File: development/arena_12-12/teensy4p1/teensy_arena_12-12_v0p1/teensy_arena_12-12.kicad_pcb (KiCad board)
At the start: 4 copper layers, 228.6 x 228.6 mm, 51 parts, among them J1 Barrel_Jack, J2 Conn_01x04, J3 Conn_01x04, P1 CONN15, P10 CONN15, P11 CONN15, P12 CONN15, P2 CONN15, P3 CONN15, P4 CONN15, P5 CONN15, P6 CONN15, P7 CONN15, P8 CONN15, P9 CONN15, Q2 MOSFET_NCHAN, SW1 SW_SPDT, U1 TXB0108PW, U18 Teensy4.1, U2 TXB0108PW, U3 TXB0108PW, U4 TXB0108PW, U5 TXB0108PW

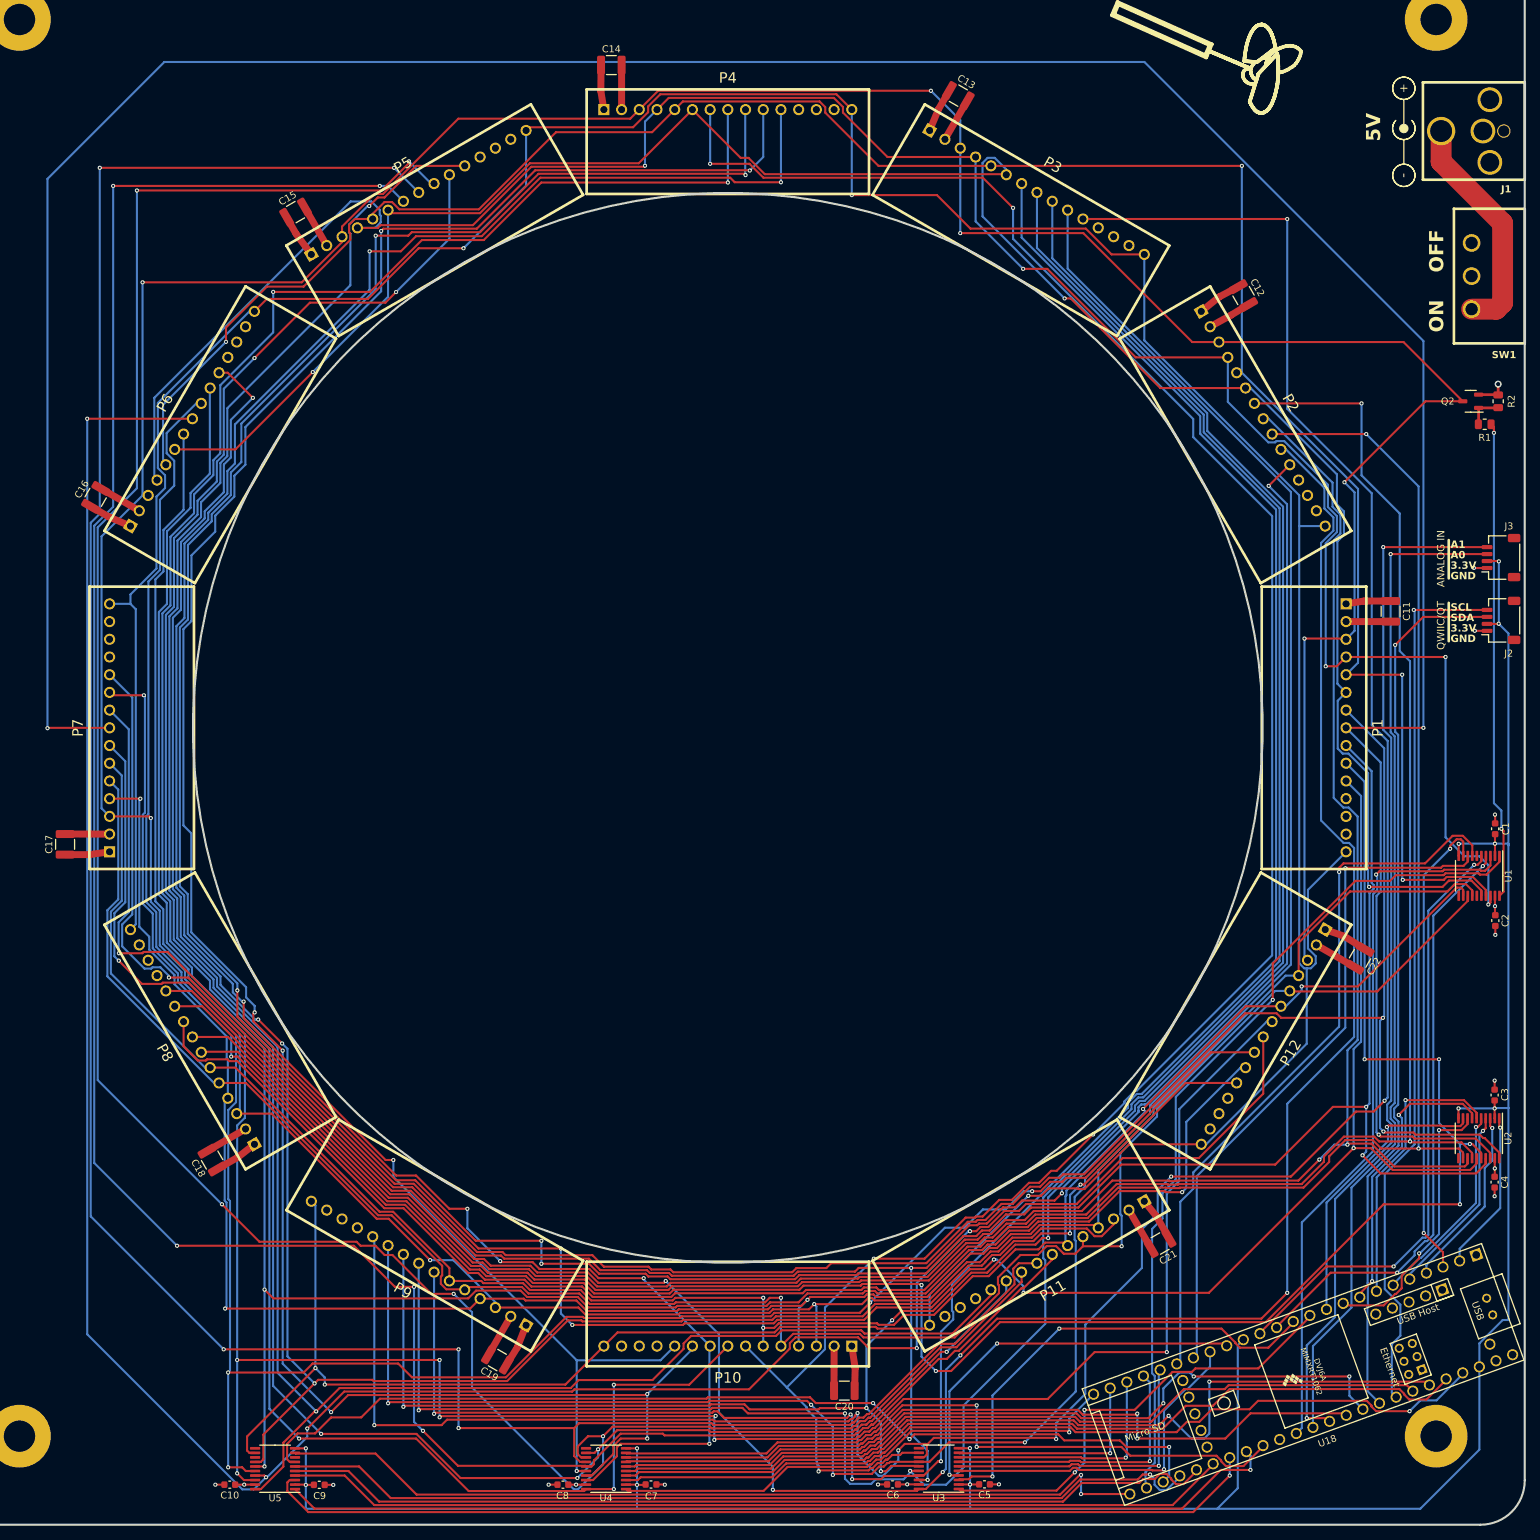
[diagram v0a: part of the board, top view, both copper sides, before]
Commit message: More work on schematic for 12-12 teensy arena.
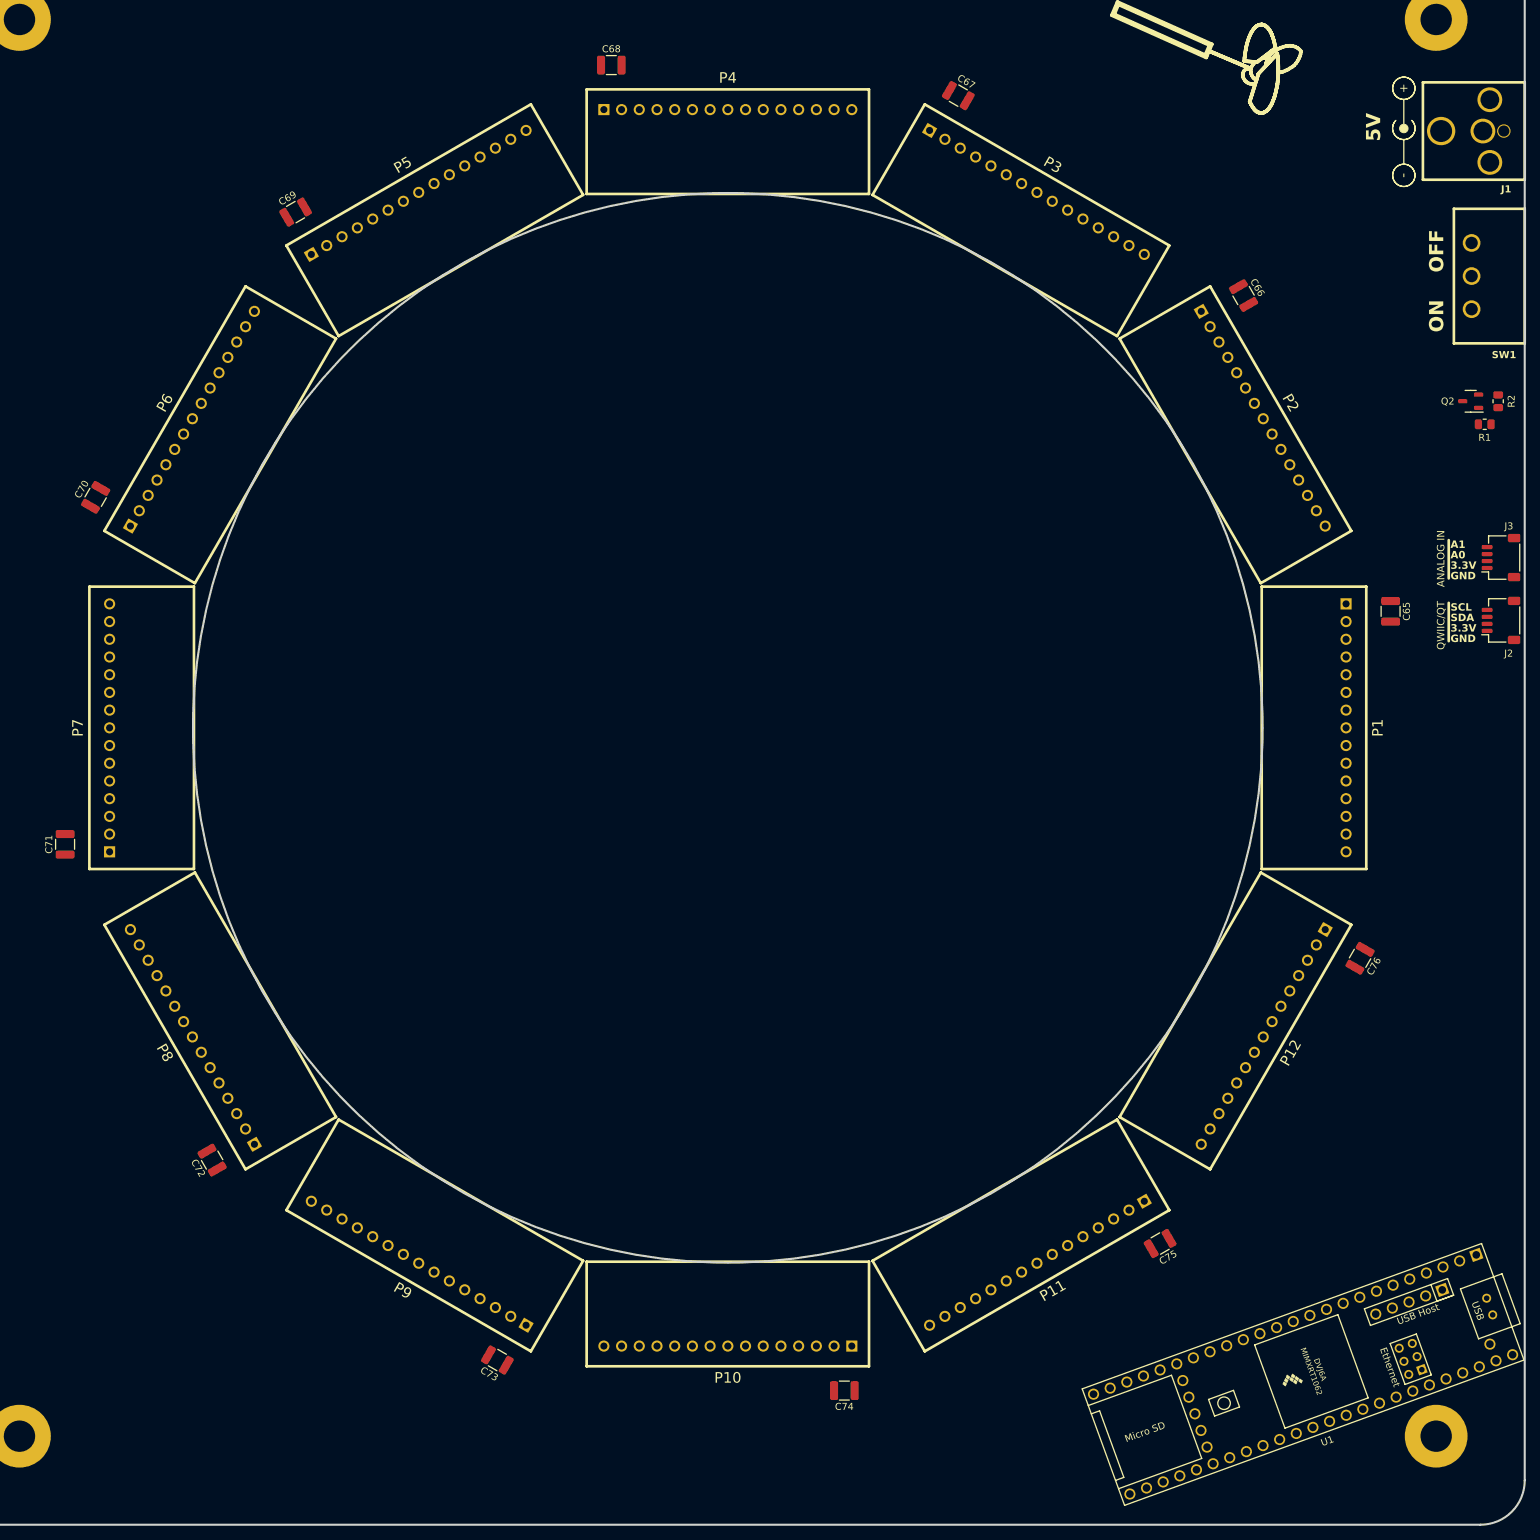
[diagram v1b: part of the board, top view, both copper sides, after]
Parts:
- removed C1, C10, C2, C3, C4, C5, C6, C7, C8, C9: 0.1uF, Capacitor_SMD:C_0603_1608Metric
- removed the U1 at (285.6, 199.0)
- removed U2, U3, U4, U5: TXB0108PW, Package_SO:TSSOP-20_4.4x6.5mm_P0.65mm
- renumbered C11 to C65, C12 to C66, C13 to C67, C14 to C68, C15 to C69, C16 to C70, C17 to C71, C18 to C72, C19 to C73, C20 to C74, C21 to C75, C22 to C76, U18 to U1
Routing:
- net /Level Shifters/PAN5V.EXT_INT: track 618.7 -> 0.00 mm, vias 5 -> 0
- net /Panel Headers/RESET: track 613.6 -> 0.00 mm, vias 8 -> 0
- net /Level Shifters/PAN5V.CS_01: track 453.8 -> 0.00 mm, vias 3 -> 0
- net +3.3V: track 394.0 -> 0.00 mm, vias 12 -> 0
- net /Level Shifters/PAN5V.CS_14: track 380.7 -> 0.00 mm, vias 7 -> 0
- net /Level Shifters/PAN5V.CS_21: track 370.7 -> 0.00 mm, vias 5 -> 0
- net /Level Shifters/PAN5V.CS_26: track 365.6 -> 0.00 mm, vias 5 -> 0
- net /Level Shifters/PAN5V.CS_25: track 364.2 -> 0.00 mm, vias 7 -> 0
- net /Level Shifters/PAN5V.CS_20: track 364.1 -> 0.00 mm, vias 5 -> 0
- net /Level Shifters/PAN5V.CS_22: track 361.9 -> 0.00 mm, vias 5 -> 0
- net /Level Shifters/PAN5V.CS_03: track 354.9 -> 0.00 mm, vias 8 -> 0
- net /Level Shifters/PAN5V.CS_08: track 348.9 -> 0.00 mm, vias 5 -> 0
- net /Level Shifters/PAN5V.CS_16: track 343.3 -> 0.00 mm, vias 5 -> 0
- net /Level Shifters/PAN5V.CS_27: track 335.3 -> 0.00 mm, vias 4 -> 0
- net /Level Shifters/PAN5V.CS_04: track 334.9 -> 0.00 mm, vias 6 -> 0
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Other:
- copper layers 4 -> 6

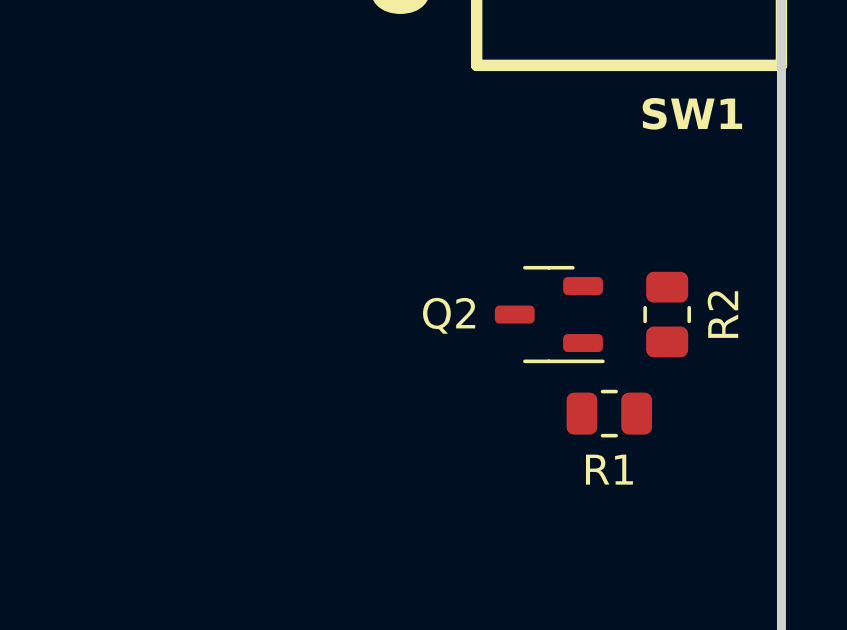
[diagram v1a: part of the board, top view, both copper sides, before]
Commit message: Reworked schematic for 12-12 teensy arena w/o regulators some more.
Worked on foot print assignmets. Started replacing some of the single
schmitt triggers with equivalent dual versions to reduce component
count.
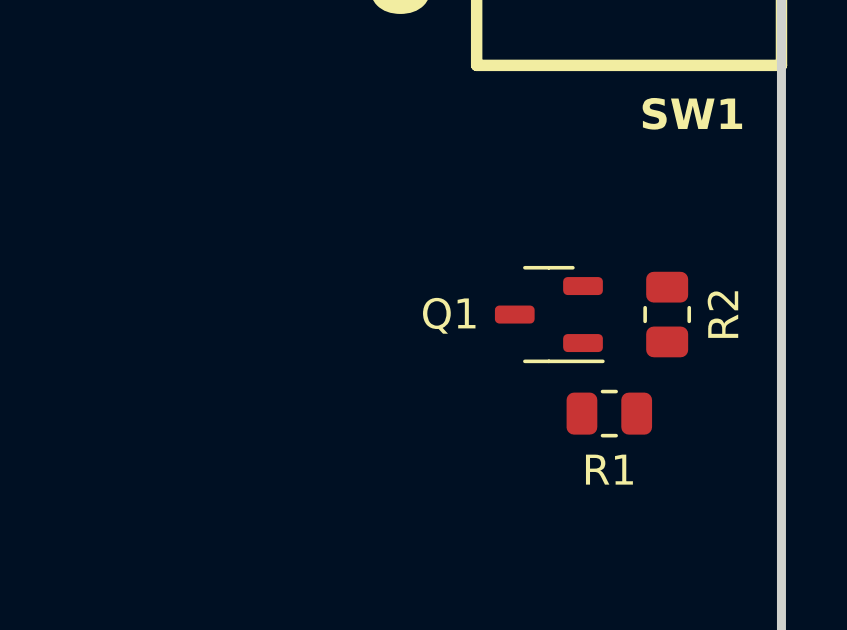
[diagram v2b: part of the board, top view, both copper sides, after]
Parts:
- renumbered Q2 to Q1
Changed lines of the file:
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@@
 		(descr "SOT, 3 Pin (https://www.jedec.org/sites/default/files/docs/Mo-178D.PDF inferred 3-pin variant), generated with kicad-footprint-generator ipc_gullwing_generator.py")
 		(tags "SOT TO_SOT_SMD")
-		(property "Reference" "Q2"
+		(property "Reference" "Q1"
 			(at 3.2965 0 0)
 			(layer "F.SilkS")
@@
 			(at 0 2.4 0)
 			(layer "F.Fab")
+			(hide yes)
 			(effects
 				(font
@@
 			(at 0 1.65 90)
 			(layer "F.Fab")
+			(hide yes)
 			(effects
 				(font
@@
 		)
 		(property "Footprint" ""
-			(at 0 0 -90)
+			(at 0 0 90)
 			(layer "F.Fab")
 			(hide yes)
@@
 		)
 		(property "Datasheet" ""
-			(at 0 0 -90)
+			(at 0 0 90)
 			(layer "F.Fab")
 			(hide yes)
@@
 		)
 		(property "Description" "Resistor"
-			(at 0 0 -90)
+			(at 0 0 90)
 			(layer "F.Fab")
 			(hide yes)

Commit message: Finished initial schematic for 12-12 teensy 4.1 arena w/o vreg.
Finished footprint assignments and started working on layout changes.
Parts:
- added C1: 0.1uF, Capacitor_SMD:C_0603_1608Metric, F.Cu at (-13.2, 115.5)
- added C10: 0.1uF, Capacitor_SMD:C_0603_1608Metric, F.Cu at (-71.9, 135.6)
- added C11: 0.1uF, Capacitor_SMD:C_0603_1608Metric, F.Cu at (-71.9, 138.1)
- added C12: 0.1uF, Capacitor_SMD:C_0603_1608Metric, F.Cu at (-71.9, 140.6)
- added C13: 0.1uF, Capacitor_SMD:C_0603_1608Metric, F.Cu at (-71.9, 143.1)
- added C14: 0.1uF, Capacitor_SMD:C_0603_1608Metric, F.Cu at (-71.9, 145.6)
- added C15: 0.1uF, Capacitor_SMD:C_0603_1608Metric, F.Cu at (-71.9, 148.1)
- added C16: 0.1uF, Capacitor_SMD:C_0603_1608Metric, F.Cu at (-71.9, 150.6)
- added C17: 0.1uF, Capacitor_SMD:C_0603_1608Metric, F.Cu at (-67.9, 115.5)
- added C18: 0.1uF, Capacitor_SMD:C_0603_1608Metric, F.Cu at (-67.9, 118.0)
- added C19: 0.1uF, Capacitor_SMD:C_0603_1608Metric, F.Cu at (-67.9, 120.5)
- added C2: 0.1uF, Capacitor_SMD:C_0603_1608Metric, F.Cu at (-71.9, 115.5)
- added C20: 0.1uF, Capacitor_SMD:C_0603_1608Metric, F.Cu at (-67.9, 123.0)
- added C21: 0.1uF, Capacitor_SMD:C_0603_1608Metric, F.Cu at (-67.9, 125.5)
- added C22: 0.1uF, Capacitor_SMD:C_0603_1608Metric, F.Cu at (-67.9, 128.0)
- added C23: 0.1uF, Capacitor_SMD:C_0603_1608Metric, F.Cu at (-67.9, 130.5)
- added C24: 0.1uF, Capacitor_SMD:C_0603_1608Metric, F.Cu at (-67.9, 133.1)
- added C25: 0.1uF, Capacitor_SMD:C_0603_1608Metric, F.Cu at (-67.9, 135.6)
- added C26: 0.1uF, Capacitor_SMD:C_0603_1608Metric, F.Cu at (-67.9, 138.1)
- added C27: 0.1uF, Capacitor_SMD:C_0603_1608Metric, F.Cu at (-67.9, 140.6)
- added C28: 0.1uF, Capacitor_SMD:C_0603_1608Metric, F.Cu at (-67.9, 143.1)
- added C29: 0.1uF, Capacitor_SMD:C_0603_1608Metric, F.Cu at (-67.9, 145.6)
- added C3: 0.1uF, Capacitor_SMD:C_0603_1608Metric, F.Cu at (-71.9, 118.0)
- added C30: 0.1uF, Capacitor_SMD:C_0603_1608Metric, F.Cu at (-67.9, 148.1)
- added C31: 0.1uF, Capacitor_SMD:C_0603_1608Metric, F.Cu at (-67.9, 150.6)
- added C32: 0.1uF, Capacitor_SMD:C_0603_1608Metric, F.Cu at (-63.8, 115.5)
- added C33: 0.1uF, Capacitor_SMD:C_0603_1608Metric, F.Cu at (-63.8, 118.0)
- added C34: 0.1uF, Capacitor_SMD:C_0603_1608Metric, F.Cu at (-63.8, 120.5)
- added C35: 0.1uF, Capacitor_SMD:C_0603_1608Metric, F.Cu at (-63.8, 123.0)
- added C36: 0.1uF, Capacitor_SMD:C_0603_1608Metric, F.Cu at (-63.8, 125.5)
- added C37: 0.1uF, Capacitor_SMD:C_0603_1608Metric, F.Cu at (-63.8, 128.0)
- added C38: 0.1uF, Capacitor_SMD:C_0603_1608Metric, F.Cu at (-63.8, 130.5)
- added C39: 0.1uF, Capacitor_SMD:C_0603_1608Metric, F.Cu at (-63.8, 133.1)
- added C4: 0.1uF, Capacitor_SMD:C_0603_1608Metric, F.Cu at (-71.9, 120.5)
- added C40: 0.1uF, Capacitor_SMD:C_0603_1608Metric, F.Cu at (-63.8, 135.6)
- added C41: 0.1uF, Capacitor_SMD:C_0603_1608Metric, F.Cu at (-63.8, 138.1)
- added C42: 0.1uF, Capacitor_SMD:C_0603_1608Metric, F.Cu at (-63.8, 140.6)
- added C43: 0.1uF, Capacitor_SMD:C_0603_1608Metric, F.Cu at (-63.8, 143.1)
- added C44: 0.1uF, Capacitor_SMD:C_0603_1608Metric, F.Cu at (-63.8, 145.6)
- added C45: 0.1uF, Capacitor_SMD:C_0603_1608Metric, F.Cu at (-63.8, 148.1)
- added C46: 0.1uF, Capacitor_SMD:C_0603_1608Metric, F.Cu at (-63.8, 150.6)
- added C47: 0.1uF, Capacitor_SMD:C_0603_1608Metric, F.Cu at (-71.9, 70.8)
- added C48: 0.1uF, Capacitor_SMD:C_0603_1608Metric, F.Cu at (-71.9, 73.3)
- added C49: 0.1uF, Capacitor_SMD:C_0603_1608Metric, F.Cu at (-71.9, 75.8)
- added C5: 0.1uF, Capacitor_SMD:C_0603_1608Metric, F.Cu at (-71.9, 123.0)
- added C50: 0.1uF, Capacitor_SMD:C_0603_1608Metric, F.Cu at (-71.9, 78.3)
- added C51: 0.1uF, Capacitor_SMD:C_0603_1608Metric, F.Cu at (-71.9, 80.9)
- added C52: 0.1uF, Capacitor_SMD:C_0603_1608Metric, F.Cu at (-71.9, 83.4)
- added C53: 0.1uF, Capacitor_SMD:C_0603_1608Metric, F.Cu at (-71.9, 85.9)
- added C54: 0.1uF, Capacitor_SMD:C_0603_1608Metric, F.Cu at (-71.9, 88.4)
- added C55: 0.1uF, Capacitor_SMD:C_0603_1608Metric, F.Cu at (-71.9, 90.9)
- added C56: 0.1uF, Capacitor_SMD:C_0603_1608Metric, F.Cu at (-71.9, 93.4)
- added C57: 0.1uF, Capacitor_SMD:C_0603_1608Metric, F.Cu at (-71.9, 95.9)
- added C58: 0.1uF, Capacitor_SMD:C_0603_1608Metric, F.Cu at (-71.9, 98.4)
- added C59: 0.1uF, Capacitor_SMD:C_0603_1608Metric, F.Cu at (-71.9, 100.9)
- added C6: 0.1uF, Capacitor_SMD:C_0603_1608Metric, F.Cu at (-71.9, 125.5)
- added C60: 0.1uF, Capacitor_SMD:C_0603_1608Metric, F.Cu at (-71.9, 103.4)
- added C61: 0.1uF, Capacitor_SMD:C_0603_1608Metric, F.Cu at (-71.9, 106.0)
- added C62: 0.1uF, Capacitor_SMD:C_0603_1608Metric, F.Cu at (-71.9, 108.5)
- added C63: 0.1uF, Capacitor_SMD:C_0603_1608Metric, F.Cu at (-71.9, 111.0)
- added C64: 0.1uF, Capacitor_SMD:C_0603_1608Metric, F.Cu at (-67.9, 70.8)
- added C65: 0.1uF, Capacitor_SMD:C_0603_1608Metric, F.Cu at (-67.9, 73.3)
- added C66: 0.1uF, Capacitor_SMD:C_0603_1608Metric, F.Cu at (-67.9, 75.8)
- added C67: 0.1uF, Capacitor_SMD:C_0603_1608Metric, F.Cu at (-67.9, 78.3)
- added C68: 0.1uF, Capacitor_SMD:C_0603_1608Metric, F.Cu at (-67.9, 80.9)
- added C69: 0.1uF, Capacitor_SMD:C_0603_1608Metric, F.Cu at (-67.9, 83.4)
- added C7: 0.1uF, Capacitor_SMD:C_0603_1608Metric, F.Cu at (-71.9, 128.0)
- added C70: 0.1uF, Capacitor_SMD:C_0603_1608Metric, F.Cu at (-67.9, 85.9)
- added C71: 0.1uF, Capacitor_SMD:C_0603_1608Metric, F.Cu at (-67.9, 88.4)
- added C72: 0.1uF, Capacitor_SMD:C_0603_1608Metric, F.Cu at (-67.9, 90.9)
- added C73: 0.1uF, Capacitor_SMD:C_0603_1608Metric, F.Cu at (-67.9, 93.4)
- added C74: 0.1uF, Capacitor_SMD:C_0603_1608Metric, F.Cu at (-67.9, 95.9)
- added C75: 0.1uF, Capacitor_SMD:C_0603_1608Metric, F.Cu at (-67.9, 98.4)
- added C76: 0.1uF, Capacitor_SMD:C_0603_1608Metric, F.Cu at (-67.9, 100.9)
- added C77: 0.1uF, Capacitor_SMD:C_0603_1608Metric, F.Cu at (-67.9, 103.4)
- added C78: 0.1uF, Capacitor_SMD:C_0603_1608Metric, F.Cu at (-67.9, 106.0)
- added C79: 0.1uF, Capacitor_SMD:C_0603_1608Metric, F.Cu at (-67.9, 108.5)
- added C8: 0.1uF, Capacitor_SMD:C_0603_1608Metric, F.Cu at (-71.9, 130.5)
- added C80: 0.1uF, Capacitor_SMD:C_0603_1608Metric, F.Cu at (-67.9, 111.0)
- added C81: 0.1uF, Capacitor_SMD:C_0603_1608Metric, F.Cu at (-63.8, 70.8)
- added C82: 0.1uF, Capacitor_SMD:C_0603_1608Metric, F.Cu at (-63.8, 73.3)
- added C83: 0.1uF, Capacitor_SMD:C_0603_1608Metric, F.Cu at (-63.8, 75.8)
- added C84: 0.1uF, Capacitor_SMD:C_0603_1608Metric, F.Cu at (-63.8, 78.3)
- added C85: 0.1uF, Capacitor_SMD:C_0603_1608Metric, F.Cu at (-63.8, 80.9)
- added C86: 0.1uF, Capacitor_SMD:C_0603_1608Metric, F.Cu at (-63.8, 83.4)
- added C87: 0.1uF, Capacitor_SMD:C_0603_1608Metric, F.Cu at (-63.8, 85.9)
- added C88: 0.1uF, Capacitor_SMD:C_0603_1608Metric, F.Cu at (-63.8, 88.4)
- added C89: 0.1uF, Capacitor_SMD:C_0603_1608Metric, F.Cu at (-63.8, 90.9)
- added C9: 0.1uF, Capacitor_SMD:C_0603_1608Metric, F.Cu at (-71.9, 133.1)
- added C90: 0.1uF, Capacitor_SMD:C_0603_1608Metric, F.Cu at (-63.8, 93.4)
- added C91: 0.1uF, Capacitor_SMD:C_0603_1608Metric, F.Cu at (-63.8, 95.9)
- added C92: 0.1uF, Capacitor_SMD:C_0603_1608Metric, F.Cu at (-63.8, 98.4)
- added C93: 0.1uF, Capacitor_SMD:C_0603_1608Metric, F.Cu at (-63.8, 100.9)
- added C94: 0.1uF, Capacitor_SMD:C_0603_1608Metric, F.Cu at (-63.8, 103.4)
- added J4: Barrel_Jack, arena_custom:DCJACK_2PIN_HIGHCURRENT, F.Cu at (95.0, 63.5)
- added Q1: MOSFET_NCHAN, Package_TO_SOT_SMD:SOT-23-3, F.Cu at (-35.2, 71.8)
- added R10: 68, Resistor_SMD:R_0603_1608Metric, F.Cu at (275.6, 253.6)
- added R100: 68, Resistor_SMD:R_0603_1608Metric, F.Cu at (-43.8, 118.0)
- added R101: 68, Resistor_SMD:R_0603_1608Metric, F.Cu at (-43.8, 120.5)
- added R102: 68, Resistor_SMD:R_0603_1608Metric, F.Cu at (-43.8, 123.0)
- added R103: 68, Resistor_SMD:R_0603_1608Metric, F.Cu at (-43.8, 125.5)
- added R104: 68, Resistor_SMD:R_0603_1608Metric, F.Cu at (-43.8, 128.0)
- added R105: 68, Resistor_SMD:R_0603_1608Metric, F.Cu at (-43.8, 130.5)
- added R106: 68, Resistor_SMD:R_0603_1608Metric, F.Cu at (-43.8, 133.1)
- added R107: 68, Resistor_SMD:R_0603_1608Metric, F.Cu at (-43.8, 135.6)
- added R108: 68, Resistor_SMD:R_0603_1608Metric, F.Cu at (-43.8, 138.1)
- added R109: 68, Resistor_SMD:R_0603_1608Metric, F.Cu at (-43.8, 140.6)
- added R11: 68, Resistor_SMD:R_0603_1608Metric, F.Cu at (273.2, 254.3)
- added R110: 68, Resistor_SMD:R_0603_1608Metric, F.Cu at (-43.8, 143.1)
- added R111: 68, Resistor_SMD:R_0603_1608Metric, F.Cu at (-43.8, 145.6)
- added R112: 68, Resistor_SMD:R_0603_1608Metric, F.Cu at (-43.8, 148.1)
- added R113: 68, Resistor_SMD:R_0603_1608Metric, F.Cu at (-43.8, 150.6)
- added R114: 68, Resistor_SMD:R_0603_1608Metric, F.Cu at (-39.8, 115.5)
- added R115: 68, Resistor_SMD:R_0603_1608Metric, F.Cu at (-39.8, 118.0)
- added R116: 68, Resistor_SMD:R_0603_1608Metric, F.Cu at (-39.8, 120.5)
- added R117: 68, Resistor_SMD:R_0603_1608Metric, F.Cu at (-39.8, 123.0)
- added R118: 68, Resistor_SMD:R_0603_1608Metric, F.Cu at (-39.8, 125.5)
- added R119: 68, Resistor_SMD:R_0603_1608Metric, F.Cu at (-39.8, 128.0)
- added R12: 68, Resistor_SMD:R_0603_1608Metric, F.Cu at (-9.16, 120.5)
- added R120: 68, Resistor_SMD:R_0603_1608Metric, F.Cu at (-39.8, 130.5)
- added R121: 68, Resistor_SMD:R_0603_1608Metric, F.Cu at (-39.8, 133.1)
- added R122: 68, Resistor_SMD:R_0603_1608Metric, F.Cu at (-39.8, 135.6)
- added R123: 68, Resistor_SMD:R_0603_1608Metric, F.Cu at (-39.8, 138.1)
- added R124: 68, Resistor_SMD:R_0603_1608Metric, F.Cu at (-39.8, 140.6)
- added R125: 68, Resistor_SMD:R_0603_1608Metric, F.Cu at (-39.8, 143.1)
- added R126: 68, Resistor_SMD:R_0603_1608Metric, F.Cu at (-39.8, 145.6)
- added R127: 68, Resistor_SMD:R_0603_1608Metric, F.Cu at (-63.8, 106.0)
- added R128: 68, Resistor_SMD:R_0603_1608Metric, F.Cu at (-63.8, 108.5)
- added R129: 68, Resistor_SMD:R_0603_1608Metric, F.Cu at (300.2, 208.7)
- added R13: 68, Resistor_SMD:R_0603_1608Metric, F.Cu at (-9.16, 123.0)
- added R130: 68, Resistor_SMD:R_0603_1608Metric, F.Cu at (-59.8, 70.8)
- added R131: 68, Resistor_SMD:R_0603_1608Metric, F.Cu at (-59.8, 73.3)
- added R132: 68, Resistor_SMD:R_0603_1608Metric, F.Cu at (304.2, 173.5)
- added R133: 68, Resistor_SMD:R_0603_1608Metric, F.Cu at (271.9, 185.4)
- added R134: 68, Resistor_SMD:R_0603_1608Metric, F.Cu at (271.5, 194.3)
- added R135: 68, Resistor_SMD:R_0603_1608Metric, F.Cu at (-59.8, 83.4)
- added R136: 68, Resistor_SMD:R_0603_1608Metric, F.Cu at (-59.8, 85.9)
- added R137: 68, Resistor_SMD:R_0603_1608Metric, F.Cu at (-59.8, 88.4)
- added R138: 68, Resistor_SMD:R_0603_1608Metric, F.Cu at (-59.8, 90.9)
- added R139: 68, Resistor_SMD:R_0603_1608Metric, F.Cu at (-59.8, 93.4)
- added R14: 68, Resistor_SMD:R_0603_1608Metric, F.Cu at (-9.16, 125.5)
- added R140: 68, Resistor_SMD:R_0603_1608Metric, F.Cu at (-59.8, 95.9)
- added R141: 68, Resistor_SMD:R_0603_1608Metric, F.Cu at (-59.8, 98.4)
- added R142: 68, Resistor_SMD:R_0603_1608Metric, F.Cu at (-59.8, 100.9)
- added R143: 68, Resistor_SMD:R_0603_1608Metric, F.Cu at (-59.8, 103.4)
- added R144: 68, Resistor_SMD:R_0603_1608Metric, F.Cu at (-59.8, 106.0)
- added R145: 68, Resistor_SMD:R_0603_1608Metric, F.Cu at (-59.8, 108.5)
- added R146: 68, Resistor_SMD:R_0603_1608Metric, F.Cu at (-59.8, 111.0)
- added R147: 68, Resistor_SMD:R_0603_1608Metric, F.Cu at (-55.8, 70.8)
- added R148: 68, Resistor_SMD:R_0603_1608Metric, F.Cu at (-55.8, 73.3)
- added R149: 68, Resistor_SMD:R_0603_1608Metric, F.Cu at (-55.8, 75.8)
- added R15: 68, Resistor_SMD:R_0603_1608Metric, F.Cu at (-9.16, 128.0)
- added R150: 68, Resistor_SMD:R_0603_1608Metric, F.Cu at (-55.8, 78.3)
- added R151: 68, Resistor_SMD:R_0603_1608Metric, F.Cu at (-55.8, 80.9)
- added R152: 68, Resistor_SMD:R_0603_1608Metric, F.Cu at (-55.8, 83.4)
- added R153: 68, Resistor_SMD:R_0603_1608Metric, F.Cu at (-55.8, 85.9)
- added R154: 68, Resistor_SMD:R_0603_1608Metric, F.Cu at (-55.8, 88.4)
- added R155: 68, Resistor_SMD:R_0603_1608Metric, F.Cu at (-55.8, 90.9)
- added R156: 68, Resistor_SMD:R_0603_1608Metric, F.Cu at (-55.8, 93.4)
- added R157: 68, Resistor_SMD:R_0603_1608Metric, F.Cu at (-55.8, 95.9)
- added R158: 68, Resistor_SMD:R_0603_1608Metric, F.Cu at (-55.8, 98.4)
- added R159: 68, Resistor_SMD:R_0603_1608Metric, F.Cu at (-55.8, 100.9)
- added R16: 68, Resistor_SMD:R_0603_1608Metric, F.Cu at (-9.16, 130.5)
- added R160: 68, Resistor_SMD:R_0603_1608Metric, F.Cu at (-55.8, 103.4)
- added R161: 68, Resistor_SMD:R_0603_1608Metric, F.Cu at (-55.8, 106.0)
- added R162: 68, Resistor_SMD:R_0603_1608Metric, F.Cu at (-55.8, 108.5)
- added R163: 68, Resistor_SMD:R_0603_1608Metric, F.Cu at (-55.8, 111.0)
- added R164: 68, Resistor_SMD:R_0603_1608Metric, F.Cu at (-51.8, 70.8)
- added R165: 68, Resistor_SMD:R_0603_1608Metric, F.Cu at (-51.8, 73.3)
- added R166: 68, Resistor_SMD:R_0603_1608Metric, F.Cu at (-51.8, 75.8)
- added R167: 68, Resistor_SMD:R_0603_1608Metric, F.Cu at (-51.8, 78.3)
- added R168: 68, Resistor_SMD:R_0603_1608Metric, F.Cu at (-51.8, 80.9)
- added R169: 68, Resistor_SMD:R_0603_1608Metric, F.Cu at (-51.8, 83.4)
- added R17: 68, Resistor_SMD:R_0603_1608Metric, F.Cu at (-9.16, 133.1)
- added R170: 68, Resistor_SMD:R_0603_1608Metric, F.Cu at (-51.8, 85.9)
- added R171: 68, Resistor_SMD:R_0603_1608Metric, F.Cu at (-51.8, 88.4)
- added R172: 68, Resistor_SMD:R_0603_1608Metric, F.Cu at (-51.8, 90.9)
- added R173: 68, Resistor_SMD:R_0603_1608Metric, F.Cu at (-51.8, 93.4)
- added R174: 68, Resistor_SMD:R_0603_1608Metric, F.Cu at (-51.8, 95.9)
- added R175: 68, Resistor_SMD:R_0603_1608Metric, F.Cu at (-51.8, 98.4)
- added R176: 68, Resistor_SMD:R_0603_1608Metric, F.Cu at (-51.8, 100.9)
- added R177: 68, Resistor_SMD:R_0603_1608Metric, F.Cu at (-51.8, 103.4)
- added R178: 68, Resistor_SMD:R_0603_1608Metric, F.Cu at (-51.8, 106.0)
- added R179: 68, Resistor_SMD:R_0603_1608Metric, F.Cu at (-51.8, 108.5)
- added R18: 68, Resistor_SMD:R_0603_1608Metric, F.Cu at (-5.15, 115.5)
- added R180: 68, Resistor_SMD:R_0603_1608Metric, F.Cu at (-51.8, 111.0)
- added R181: 68, Resistor_SMD:R_0603_1608Metric, F.Cu at (-47.8, 70.8)
- added R182: 68, Resistor_SMD:R_0603_1608Metric, F.Cu at (-47.8, 73.3)
- added R183: 68, Resistor_SMD:R_0603_1608Metric, F.Cu at (-47.8, 75.8)
- added R184: 68, Resistor_SMD:R_0603_1608Metric, F.Cu at (-47.8, 78.3)
- added R185: 68, Resistor_SMD:R_0603_1608Metric, F.Cu at (-47.8, 80.9)
- added R186: 68, Resistor_SMD:R_0603_1608Metric, F.Cu at (-47.8, 83.4)
- added R187: 68, Resistor_SMD:R_0603_1608Metric, F.Cu at (-47.8, 85.9)
- added R188: 68, Resistor_SMD:R_0603_1608Metric, F.Cu at (-47.8, 88.4)
- added R189: 68, Resistor_SMD:R_0603_1608Metric, F.Cu at (-47.8, 90.9)
- added R19: 68, Resistor_SMD:R_0603_1608Metric, F.Cu at (-5.15, 118.0)
- added R190: 68, Resistor_SMD:R_0603_1608Metric, F.Cu at (-47.8, 93.4)
- added R191: 68, Resistor_SMD:R_0603_1608Metric, F.Cu at (-47.8, 95.9)
- added R192: 68, Resistor_SMD:R_0603_1608Metric, F.Cu at (-47.8, 98.4)
- added R193: 68, Resistor_SMD:R_0603_1608Metric, F.Cu at (-47.8, 100.9)
- added R194: 68, Resistor_SMD:R_0603_1608Metric, F.Cu at (-47.8, 103.4)
- added R195: 68, Resistor_SMD:R_0603_1608Metric, F.Cu at (-47.8, 106.0)
- added R196: 68, Resistor_SMD:R_0603_1608Metric, F.Cu at (-47.8, 108.5)
- added R197: 68, Resistor_SMD:R_0603_1608Metric, F.Cu at (-47.8, 111.0)
- added R198: 68, Resistor_SMD:R_0603_1608Metric, F.Cu at (-43.8, 70.8)
- added R199: 68, Resistor_SMD:R_0603_1608Metric, F.Cu at (-43.8, 73.3)
- added R20: 68, Resistor_SMD:R_0603_1608Metric, F.Cu at (-5.15, 120.5)
- added R200: 68, Resistor_SMD:R_0603_1608Metric, F.Cu at (-43.8, 75.8)
- added R201: 68, Resistor_SMD:R_0603_1608Metric, F.Cu at (-43.8, 78.3)
- added R202: 68, Resistor_SMD:R_0603_1608Metric, F.Cu at (-43.8, 80.9)
- added R203: 68, Resistor_SMD:R_0603_1608Metric, F.Cu at (-43.8, 83.4)
- added R204: 68, Resistor_SMD:R_0603_1608Metric, F.Cu at (-43.8, 85.9)
- added R205: 68, Resistor_SMD:R_0603_1608Metric, F.Cu at (-43.8, 88.4)
- added R206: 68, Resistor_SMD:R_0603_1608Metric, F.Cu at (-43.8, 90.9)
- added R207: 68, Resistor_SMD:R_0603_1608Metric, F.Cu at (-43.8, 93.4)
- added R208: 68, Resistor_SMD:R_0603_1608Metric, F.Cu at (-43.8, 95.9)
- added R209: 68, Resistor_SMD:R_0603_1608Metric, F.Cu at (-43.8, 98.4)
- added R21: 68, Resistor_SMD:R_0603_1608Metric, F.Cu at (-5.15, 123.0)
- added R210: 68, Resistor_SMD:R_0603_1608Metric, F.Cu at (-43.8, 100.9)
- added R211: 68, Resistor_SMD:R_0603_1608Metric, F.Cu at (-43.8, 103.4)
- added R212: 68, Resistor_SMD:R_0603_1608Metric, F.Cu at (-43.8, 106.0)
- added R213: 68, Resistor_SMD:R_0603_1608Metric, F.Cu at (-43.8, 108.5)
- added R214: 68, Resistor_SMD:R_0603_1608Metric, F.Cu at (-43.8, 111.0)
- added R215: 68, Resistor_SMD:R_0603_1608Metric, F.Cu at (-39.8, 70.8)
- added R216: 68, Resistor_SMD:R_0603_1608Metric, F.Cu at (-39.8, 73.3)
- added R217: 68, Resistor_SMD:R_0603_1608Metric, F.Cu at (-39.8, 75.8)
- added R218: 68, Resistor_SMD:R_0603_1608Metric, F.Cu at (-39.8, 78.3)
- added R219: 68, Resistor_SMD:R_0603_1608Metric, F.Cu at (-39.8, 80.9)
- added R22: 68, Resistor_SMD:R_0603_1608Metric, F.Cu at (-5.15, 125.5)
- added R220: 68, Resistor_SMD:R_0603_1608Metric, F.Cu at (-39.8, 83.4)
- added R221: 68, Resistor_SMD:R_0603_1608Metric, F.Cu at (-39.8, 85.9)
- added R222: 68, Resistor_SMD:R_0603_1608Metric, F.Cu at (-39.8, 88.4)
- added R23: 68, Resistor_SMD:R_0603_1608Metric, F.Cu at (-5.15, 128.0)
- added R24: 68, Resistor_SMD:R_0603_1608Metric, F.Cu at (-5.15, 130.5)
- added R25: 68, Resistor_SMD:R_0603_1608Metric, F.Cu at (-5.15, 133.1)
- added R26: 68, Resistor_SMD:R_0603_1608Metric, F.Cu at (-1.14, 115.5)
- added R27: 68, Resistor_SMD:R_0603_1608Metric, F.Cu at (-1.14, 118.0)
- added R28: 68, Resistor_SMD:R_0603_1608Metric, F.Cu at (-1.14, 120.5)
- added R29: 68, Resistor_SMD:R_0603_1608Metric, F.Cu at (-1.14, 123.0)
- added R3: 68, Resistor_SMD:R_0603_1608Metric, F.Cu at (-13.2, 118.0)
- added R30: 68, Resistor_SMD:R_0603_1608Metric, F.Cu at (-1.14, 125.5)
- added R31: 68, Resistor_SMD:R_0603_1608Metric, F.Cu at (-1.14, 128.0)
- added R32: 68, Resistor_SMD:R_0603_1608Metric, F.Cu at (-1.14, 130.5)
- added R33: 68, Resistor_SMD:R_0603_1608Metric, F.Cu at (-1.14, 133.1)
- added R34: 68, Resistor_SMD:R_0603_1608Metric, F.Cu at (2.87, 115.5)
- added R35: 68, Resistor_SMD:R_0603_1608Metric, F.Cu at (2.87, 118.0)
- added R36: 68, Resistor_SMD:R_0603_1608Metric, F.Cu at (2.87, 120.5)
- added R37: 68, Resistor_SMD:R_0603_1608Metric, F.Cu at (2.87, 123.0)
- added R38: 68, Resistor_SMD:R_0603_1608Metric, F.Cu at (2.87, 125.5)
- added R39: 68, Resistor_SMD:R_0603_1608Metric, F.Cu at (-59.8, 115.5)
- added R4: 68, Resistor_SMD:R_0603_1608Metric, F.Cu at (259.3, 276.0)
- added R40: 68, Resistor_SMD:R_0603_1608Metric, F.Cu at (-59.8, 118.0)
- added R41: 68, Resistor_SMD:R_0603_1608Metric, F.Cu at (-59.8, 120.5)
- added R42: 68, Resistor_SMD:R_0603_1608Metric, F.Cu at (-59.8, 123.0)
- added R43: 68, Resistor_SMD:R_0603_1608Metric, F.Cu at (-59.8, 125.5)
- added R44: 68, Resistor_SMD:R_0603_1608Metric, F.Cu at (-59.8, 128.0)
- added R45: 68, Resistor_SMD:R_0603_1608Metric, F.Cu at (-59.8, 130.5)
- added R46: 68, Resistor_SMD:R_0603_1608Metric, F.Cu at (-59.8, 133.1)
- added R47: 68, Resistor_SMD:R_0603_1608Metric, F.Cu at (-59.8, 135.6)
- added R48: 68, Resistor_SMD:R_0603_1608Metric, F.Cu at (-59.8, 138.1)
- added R49: 68, Resistor_SMD:R_0603_1608Metric, F.Cu at (-59.8, 140.6)
- added R5: 68, Resistor_SMD:R_0603_1608Metric, F.Cu at (256.5, 260.4)
- added R50: 68, Resistor_SMD:R_0603_1608Metric, F.Cu at (-59.8, 143.1)
- added R51: 68, Resistor_SMD:R_0603_1608Metric, F.Cu at (-59.8, 145.6)
- added R52: 68, Resistor_SMD:R_0603_1608Metric, F.Cu at (-59.8, 148.1)
- added R53: 68, Resistor_SMD:R_0603_1608Metric, F.Cu at (-59.8, 150.6)
- added R54: 68, Resistor_SMD:R_0603_1608Metric, F.Cu at (-55.8, 115.5)
- added R55: 68, Resistor_SMD:R_0603_1608Metric, F.Cu at (-55.8, 118.0)
- added R56: 68, Resistor_SMD:R_0603_1608Metric, F.Cu at (-55.8, 120.5)
- added R57: 68, Resistor_SMD:R_0603_1608Metric, F.Cu at (-55.8, 123.0)
- added R58: 68, Resistor_SMD:R_0603_1608Metric, F.Cu at (-55.8, 125.5)
- added R59: 68, Resistor_SMD:R_0603_1608Metric, F.Cu at (-55.8, 128.0)
- added R6: 68, Resistor_SMD:R_0603_1608Metric, F.Cu at (242.3, 265.4)
- added R60: 68, Resistor_SMD:R_0603_1608Metric, F.Cu at (-55.8, 130.5)
- added R61: 68, Resistor_SMD:R_0603_1608Metric, F.Cu at (-55.8, 133.1)
- added R62: 68, Resistor_SMD:R_0603_1608Metric, F.Cu at (-55.8, 135.6)
- added R63: 68, Resistor_SMD:R_0603_1608Metric, F.Cu at (-55.8, 138.1)
- added R64: 68, Resistor_SMD:R_0603_1608Metric, F.Cu at (-55.8, 140.6)
- added R65: 68, Resistor_SMD:R_0603_1608Metric, F.Cu at (-55.8, 143.1)
- added R66: 68, Resistor_SMD:R_0603_1608Metric, F.Cu at (-55.8, 145.6)
- added R67: 68, Resistor_SMD:R_0603_1608Metric, F.Cu at (-55.8, 148.1)
- added R68: 68, Resistor_SMD:R_0603_1608Metric, F.Cu at (-55.8, 150.6)
- added R69: 68, Resistor_SMD:R_0603_1608Metric, F.Cu at (-51.8, 115.5)
- added R7: 68, Resistor_SMD:R_0603_1608Metric, F.Cu at (244.6, 264.8)
- added R70: 68, Resistor_SMD:R_0603_1608Metric, F.Cu at (-51.8, 118.0)
- added R71: 68, Resistor_SMD:R_0603_1608Metric, F.Cu at (-51.8, 120.5)
- added R72: 68, Resistor_SMD:R_0603_1608Metric, F.Cu at (-51.8, 123.0)
- added R73: 68, Resistor_SMD:R_0603_1608Metric, F.Cu at (-51.8, 125.5)
- added R74: 68, Resistor_SMD:R_0603_1608Metric, F.Cu at (-51.8, 128.0)
- added R75: 68, Resistor_SMD:R_0603_1608Metric, F.Cu at (-51.8, 130.5)
- added R76: 68, Resistor_SMD:R_0603_1608Metric, F.Cu at (-51.8, 133.1)
- added R77: 68, Resistor_SMD:R_0603_1608Metric, F.Cu at (-51.8, 135.6)
- added R78: 68, Resistor_SMD:R_0603_1608Metric, F.Cu at (-51.8, 138.1)
- added R79: 68, Resistor_SMD:R_0603_1608Metric, F.Cu at (-51.8, 140.6)
- added R8: 68, Resistor_SMD:R_0603_1608Metric, F.Cu at (282.7, 251.0)
- added R80: 68, Resistor_SMD:R_0603_1608Metric, F.Cu at (-51.8, 143.1)
- added R81: 68, Resistor_SMD:R_0603_1608Metric, F.Cu at (-51.8, 145.6)
- added R82: 68, Resistor_SMD:R_0603_1608Metric, F.Cu at (-51.8, 148.1)
- added R83: 68, Resistor_SMD:R_0603_1608Metric, F.Cu at (-51.8, 150.6)
- added R84: 68, Resistor_SMD:R_0603_1608Metric, F.Cu at (-47.8, 115.5)
- added R85: 68, Resistor_SMD:R_0603_1608Metric, F.Cu at (-47.8, 118.0)
- added R86: 68, Resistor_SMD:R_0603_1608Metric, F.Cu at (-47.8, 120.5)
- added R87: 68, Resistor_SMD:R_0603_1608Metric, F.Cu at (-47.8, 123.0)
- added R88: 68, Resistor_SMD:R_0603_1608Metric, F.Cu at (-47.8, 125.5)
- added R89: 68, Resistor_SMD:R_0603_1608Metric, F.Cu at (-47.8, 128.0)
- added R9: 68, Resistor_SMD:R_0603_1608Metric, F.Cu at (277.9, 252.7)
- added R90: 68, Resistor_SMD:R_0603_1608Metric, F.Cu at (-47.8, 130.5)
- added R91: 68, Resistor_SMD:R_0603_1608Metric, F.Cu at (-47.8, 133.1)
- added R92: 68, Resistor_SMD:R_0603_1608Metric, F.Cu at (-47.8, 135.6)
- added R93: 68, Resistor_SMD:R_0603_1608Metric, F.Cu at (-47.8, 138.1)
- added R94: 68, Resistor_SMD:R_0603_1608Metric, F.Cu at (-47.8, 140.6)
- added R95: 68, Resistor_SMD:R_0603_1608Metric, F.Cu at (-47.8, 143.1)
- added R96: 68, Resistor_SMD:R_0603_1608Metric, F.Cu at (-47.8, 145.6)
- added R97: 68, Resistor_SMD:R_0603_1608Metric, F.Cu at (-47.8, 148.1)
- added R98: 68, Resistor_SMD:R_0603_1608Metric, F.Cu at (-47.8, 150.6)
- added R99: 68, Resistor_SMD:R_0603_1608Metric, F.Cu at (-43.8, 115.5)
- added U10: TXB0108PW, Package_SO:TSSOP-20_4.4x6.5mm_P0.65mm, F.Cu at (-52.0, 164.0)
- added U11: TXB0108PW, Package_SO:TSSOP-20_4.4x6.5mm_P0.65mm, F.Cu at (-52.0, 172.0)
- added U12: TXB0108PW, Package_SO:TSSOP-20_4.4x6.5mm_P0.65mm, F.Cu at (-43.2, 155.9)
- added U13: TXB0108PW, Package_SO:TSSOP-20_4.4x6.5mm_P0.65mm, F.Cu at (-43.2, 164.0)
- added U14: TXB0108PW, Package_SO:TSSOP-20_4.4x6.5mm_P0.65mm, F.Cu at (-43.2, 172.0)
- added U15: 74LVC1G17, Package_TO_SOT_SMD:SOT-23-5, F.Cu at (-35.2, 116.5)
- added U16: 74LVC1G17, Package_TO_SOT_SMD:SOT-23-5, F.Cu at (-35.2, 120.9)
- added U17: 74LVC1G17, Package_TO_SOT_SMD:SOT-23-5, F.Cu at (-35.2, 125.4)
- added U18: 74LVC1G17, Package_TO_SOT_SMD:SOT-23-5, F.Cu at (-35.2, 129.8)
- added U19: 74LVC2G17, Package_TO_SOT_SMD:SOT-23-6, F.Cu at (-35.2, 134.3)
- added U2: 74LVC2G17, Package_TO_SOT_SMD:SOT-23-6, F.Cu at (-12.6, 136.5)
- added U20: 74LVC2G17, Package_TO_SOT_SMD:SOT-23-6, F.Cu at (-35.2, 138.7)
- added U21: 74LVC2G17, Package_TO_SOT_SMD:SOT-23-6, F.Cu at (-30.1, 116.5)
- added U22: 74LVC2G17, Package_TO_SOT_SMD:SOT-23-6, F.Cu at (-30.1, 120.9)
- renumbered C70 to C100, C71 to C101, C72 to C102, C73 to C103, C74 to C104, C75 to C105, C76 to C106, C65 to C95, C66 to C96, C67 to C97, C68 to C98, C69 to C99
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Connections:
- P1 pad 10: /Level Shifters/PAN5V.CS_03 -> /Panel Headers/HDR_CS_03_P1
- P1 pad 11: /Level Shifters/PAN5V.CS_04 -> /Panel Headers/HDR_CS_04_P1
- P1 pad 15: /Level Shifters/PAN5V.EXT_INT -> /Panel Headers/HDR_EXT_INT_P1
- P1 pad 3: /Panel Headers/RESET -> /Panel Headers/HDR_RESET
- P1 pad 4: /Level Shifters/PAN5V.SCK_0 -> /Panel Headers/HDR_SCK_0_P1
- P1 pad 5: /Level Shifters/PAN5V.MOSI_0 -> /Panel Headers/HDR_MOSI_0_P1
- P1 pad 7: /Level Shifters/PAN5V.CS_00 -> /Panel Headers/HDR_CS_00_P1
- P1 pad 8: /Level Shifters/PAN5V.CS_01 -> /Panel Headers/HDR_CS_01_P1
- P1 pad 9: /Level Shifters/PAN5V.CS_02 -> /Panel Headers/HDR_CS_02_P1
- P10 pad 10: /Level Shifters/PAN5V.CS_18 -> /Panel Headers/HDR_CS_18_P10
- P10 pad 11: /Level Shifters/PAN5V.CS_19 -> /Panel Headers/HDR_CS_19_P10
- P10 pad 15: /Level Shifters/PAN5V.EXT_INT -> /Panel Headers/HDR_EXT_INT_P10
- P10 pad 3: /Panel Headers/RESET -> /Panel Headers/HDR_RESET
- P10 pad 4: /Level Shifters/PAN5V.SCK_1 -> /Panel Headers/HDR_SCK_1_P10
- P10 pad 5: /Level Shifters/PAN5V.MOSI_1 -> /Panel Headers/HDR_MOSI_1_P10
- P10 pad 7: /Level Shifters/PAN5V.CS_15 -> /Panel Headers/HDR_CS_15_P10
- P10 pad 8: /Level Shifters/PAN5V.CS_16 -> /Panel Headers/HDR_CS_16_P10
- P10 pad 9: /Level Shifters/PAN5V.CS_17 -> /Panel Headers/HDR_CS_17_P10
- P11 pad 10: /Level Shifters/PAN5V.CS_23 -> /Panel Headers/HDR_CS_23_P11
- P11 pad 11: /Level Shifters/PAN5V.CS_24 -> /Panel Headers/HDR_CS_24_P11
- P11 pad 15: /Level Shifters/PAN5V.EXT_INT -> /Panel Headers/HDR_EXT_INT_P11
- P11 pad 3: /Panel Headers/RESET -> /Panel Headers/HDR_RESET
- P11 pad 4: /Level Shifters/PAN5V.SCK_1 -> /Panel Headers/HDR_SCK_1_P11
- P11 pad 5: /Level Shifters/PAN5V.MOSI_1 -> /Panel Headers/HDR_MOSI_1_P11
- P11 pad 7: /Level Shifters/PAN5V.CS_20 -> /Panel Headers/HDR_CS_20_P11
- P11 pad 8: /Level Shifters/PAN5V.CS_21 -> /Panel Headers/HDR_CS_21_P11
- P11 pad 9: /Level Shifters/PAN5V.CS_22 -> /Panel Headers/HDR_CS_22_P11
- P12 pad 10: /Level Shifters/PAN5V.CS_28 -> /Panel Headers/HDR_CS_28_P12
- P12 pad 11: /Level Shifters/PAN5V.CS_29 -> /Panel Headers/HDR_CS_29_P12
- P12 pad 15: /Level Shifters/PAN5V.EXT_INT -> /Panel Headers/HDR_EXT_INT_P12
- P12 pad 3: /Panel Headers/RESET -> /Panel Headers/HDR_RESET
- P12 pad 4: /Level Shifters/PAN5V.SCK_1 -> /Panel Headers/HDR_SCK_1_P12
- P12 pad 5: /Level Shifters/PAN5V.MOSI_1 -> /Panel Headers/HDR_MOSI_1_P12
- P12 pad 7: /Level Shifters/PAN5V.CS_25 -> /Panel Headers/HDR_CS_25_P12
- P12 pad 8: /Level Shifters/PAN5V.CS_26 -> /Panel Headers/HDR_CS_26_P12
- P12 pad 9: /Level Shifters/PAN5V.CS_27 -> /Panel Headers/HDR_CS_27_P12
- P2 pad 10: /Level Shifters/PAN5V.CS_08 -> /Panel Headers/HDR_CS_08_P2
- P2 pad 11: /Level Shifters/PAN5V.CS_09 -> /Panel Headers/HDR_CS_09_P2
- P2 pad 15: /Level Shifters/PAN5V.EXT_INT -> /Panel Headers/HDR_EXT_INT_P2
- P2 pad 3: /Panel Headers/RESET -> /Panel Headers/HDR_RESET
- P2 pad 4: /Level Shifters/PAN5V.SCK_0 -> /Panel Headers/HDR_SCK_0_P2
- P2 pad 5: /Level Shifters/PAN5V.MOSI_0 -> /Panel Headers/HDR_MOSI_0_P2
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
